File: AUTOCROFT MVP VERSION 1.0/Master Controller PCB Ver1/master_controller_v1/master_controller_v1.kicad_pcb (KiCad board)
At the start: 2 copper layers, 55 x 77 mm, 20 parts, among them J1 DS3231, J2 BME280, J3 ESP8266, J4 HC12, J5 HC06, J6 STM32 Bluepill, J7 Keypad, U1 LM1117-3.3, U2 LM7805_TO220, U3 EEPROM

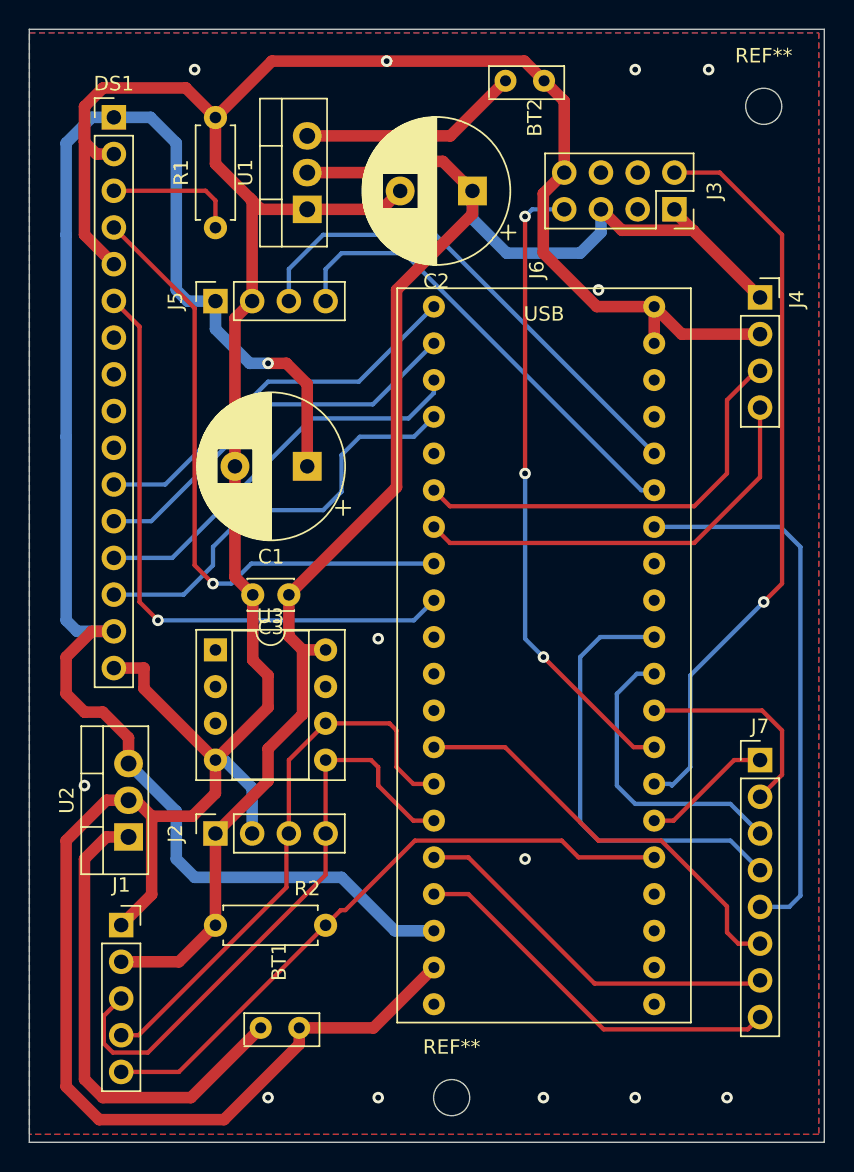
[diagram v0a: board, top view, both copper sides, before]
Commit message: Improved Silkscreen Placement
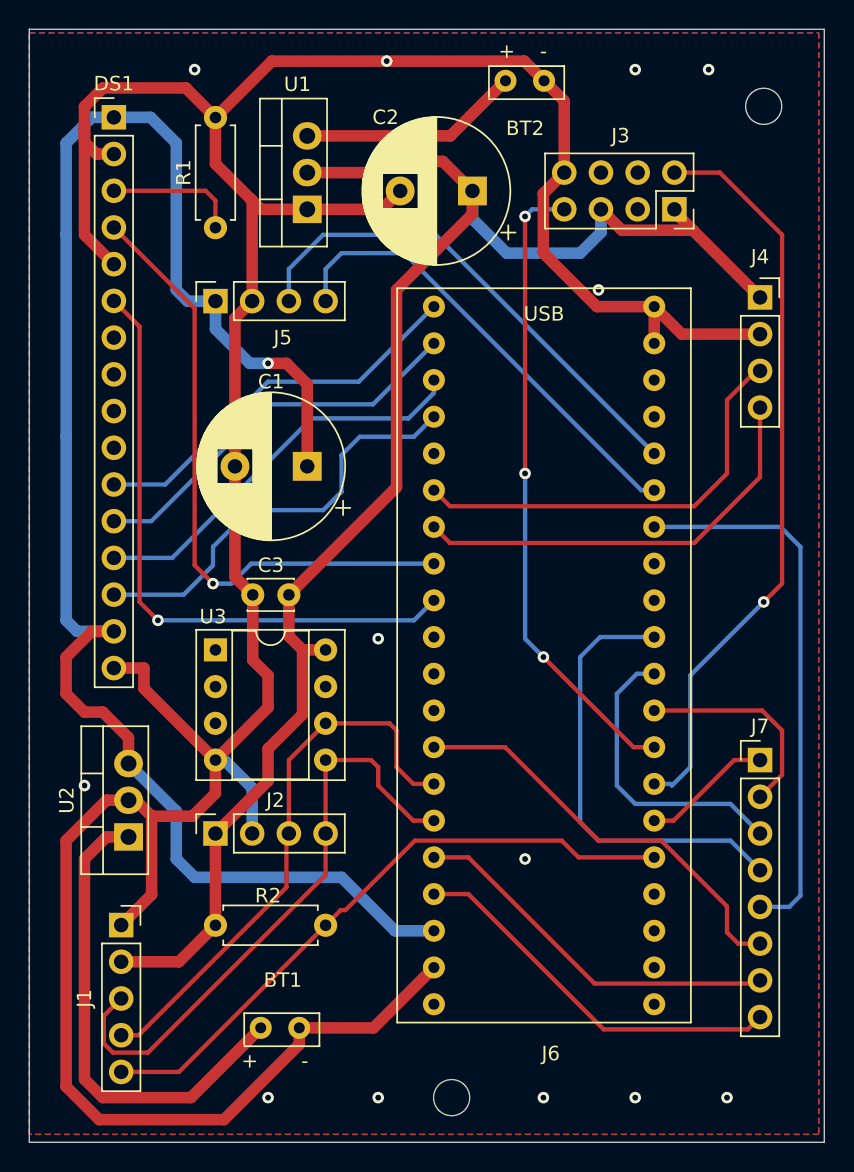
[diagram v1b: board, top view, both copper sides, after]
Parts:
-  : renamed from REF** (x2)
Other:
- board text added: "+"
- board text added: "-"

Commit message: HC12 Redesign
Accomodation of 'SET' pin for future software versions and testing.
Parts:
- J4: footprint Connector_PinSocket_2.54mm:PinSocket_1x04_P2.54mm_Vertical -> Connector_PinSocket_2.54mm:PinSocket_1x05_P2.54mm_Vertical
- moved   0.76 mm to (130.8, 99.6)
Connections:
- J6 pad 33: Net-(J6-Pad33) -> PB0
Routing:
- net PB0: track 0.00 -> 14.5 mm
- net PA2: track 51.8 -> 56.1 mm
- net PB5: track 29.2 -> 31.6 mm
- net PA9: track 29.9 -> 31.0 mm
- net PA10: track 29.7 -> 30.6 mm
- net GND: vias 13 -> 17
